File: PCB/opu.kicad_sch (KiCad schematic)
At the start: 1 part, among them J2 Conn_02x12_Odd_Even

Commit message: Modify PCB
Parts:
- added Q2: BSS84, Package_TO_SOT_SMD:SOT-23, symbol Transistor_FET:BSS84
- added Q3: BSS138, Package_TO_SOT_SMD:SOT-23, symbol Transistor_FET:BSS138
- added R2, R6: 10k, symbol Device:R
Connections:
- net DVD_LD: now also Q2.3 (D), R6.1
- net GND_LD: now also Q3.2 (S), R2.2
- net F: now reaches J2.11 (Pin_11)
- net E: now reaches J2.15 (Pin_15)
- net VR-CD: now reaches J2.17 (Pin_17)
- net VR-DVD: now reaches J2.18 (Pin_18)
- net CD-LD: now reaches J2.19 (Pin_19)
- net at J2.21 (Pin_21): now also Q2.2 (S)
- net T+: now reaches J2.3 (Pin_3)
- net T-: now reaches J2.4 (Pin_4)
- new net: Q2.1 (G), Q3.3 (D), R6.2
- new net HIGH_FREQUENCY_MODE_EN: Q3.1 (G), R2.1
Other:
- moved on the sheet: J2

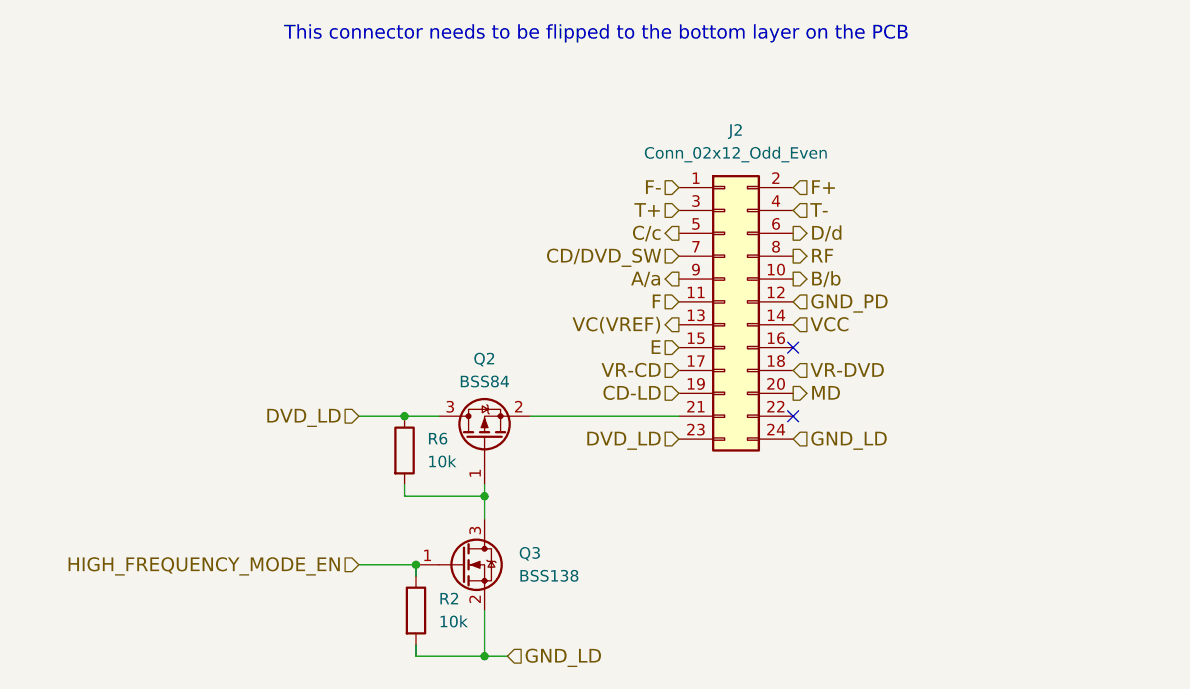
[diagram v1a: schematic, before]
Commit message: Update schematic based on testing
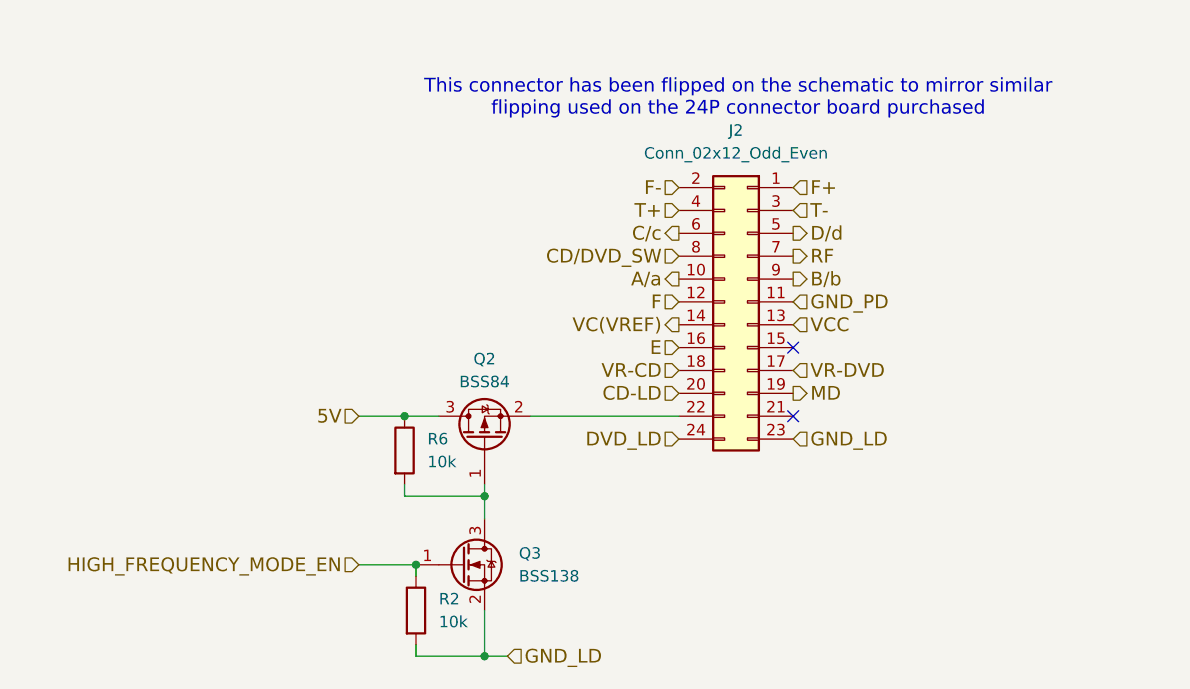
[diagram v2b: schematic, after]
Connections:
- net A/a: now also J2.10 (Pin_10); no longer J2.9 (Pin_9)
- net B/b: now also J2.9 (Pin_9); no longer J2.10 (Pin_10)
- net CD-LD: now also J2.20 (Pin_20); no longer J2.19 (Pin_19)
- net CD/DVD_SW: now also J2.8 (Pin_8); no longer J2.7 (Pin_7)
- net C/c: now also J2.6 (Pin_6); no longer J2.5 (Pin_5)
- net DVD_LD: now also J2.24 (Pin_24); no longer J2.23 (Pin_23), Q2.3 (D), R6.1
- net D/d: now also J2.5 (Pin_5); no longer J2.6 (Pin_6)
- net E: now also J2.16 (Pin_16); no longer J2.15 (Pin_15)
- net F: now also J2.12 (Pin_12); no longer J2.11 (Pin_11)
- net F+: now also J2.1 (Pin_1); no longer J2.2 (Pin_2)
- net F-: now also J2.2 (Pin_2); no longer J2.1 (Pin_1)
- net GND_LD: now also J2.23 (Pin_23); no longer J2.24 (Pin_24)
- net GND_PD: now also J2.11 (Pin_11); no longer J2.12 (Pin_12)
- net MD: now also J2.19 (Pin_19); no longer J2.20 (Pin_20)
- net RF: now also J2.7 (Pin_7); no longer J2.8 (Pin_8)
- net T+: now also J2.4 (Pin_4); no longer J2.3 (Pin_3)
- net T-: now also J2.3 (Pin_3); no longer J2.4 (Pin_4)
- net VC(VREF): now also J2.14 (Pin_14); no longer J2.13 (Pin_13)
- net VCC: now also J2.13 (Pin_13); no longer J2.14 (Pin_14)
- net VR-CD: now also J2.18 (Pin_18); no longer J2.17 (Pin_17)
- net VR-DVD: now also J2.17 (Pin_17); no longer J2.18 (Pin_18)
- net at Q2.2 (S): now also J2.22 (Pin_22); no longer J2.21 (Pin_21)
- new net 5V: Q2.3 (D), R6.1
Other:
- note added: "This connector has been flipped on the schematic to mirror similar flipping used on the 24P connector board purchased"
- note removed: "This connector needs to be flipped to the bottom layer on the PCB"
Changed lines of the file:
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@@
 	)
 	(image
-		(at 203.454 99.314)
+		(at 226.822 90.424)
 		(scale 2.27311)
 		(data "iVBORw0KGgoAAAANSUhEUgAAAloAAAF4CAIAAAADtcAdAAAAA3NCSVQICAjb4U/gAAAgAElEQVR4"
@@
 		)
 	)
-	(text "This connector needs to be flipped to the bottom layer on the PCB\n"
+	(text "This connector has been flipped on the schematic to mirror similar \nflipping used on the 24P connector board purchased\n"
 		(exclude_from_sim no)
-		(at 101.346 57.912 0)
+		(at 117.094 65.024 0)
 		(effects
 			(font
@@
 		)
 	)
-	(hierarchical_label "DVD_LD"
+	(hierarchical_label "5V"
 		(shape input)
 		(at 74.93 100.33 180)
@@
 	(symbol
 		(lib_id "Connector_Generic:Conn_02x12_Odd_Even")
-		(at 115.57 87.63 0)
+		(at 118.11 87.63 0)
+		(mirror y)
 		(unit 1)
 		(exclude_from_sim no)
@@
 		(on_board yes)
 		(dnp no)
-		(fields_autoplaced yes)
 		(property "Reference" "J2"
 			(at 116.84 68.58 0)
@@
 		)
 		(property "Footprint" "Connector_PinHeader_2.54mm:PinHeader_2x12_P2.54mm_Vertical"
-			(at 115.57 87.63 0)
+			(at 118.11 87.63 0)
 			(effects
 				(font
@@
 		)
 		(property "Datasheet" "~"
-			(at 115.57 87.63 0)
+			(at 118.11 87.63 0)
 			(effects
 				(font
@@
 		)
 		(property "Description" "Generic connector, double row, 02x12, odd/even pin numbering scheme (row 1 odd numbers, row 2 even numbers), script generated (kicad-library-utils/schlib/autogen/connector/)"
-			(at 115.57 87.63 0)
+			(at 118.11 87.63 0)
 			(effects
 				(font
